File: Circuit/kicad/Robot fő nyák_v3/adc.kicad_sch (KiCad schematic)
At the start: 9 parts, among them U28 ADC1283, U29 ADC1283, U30 ADC1283, U31 ADS1115IDGS, U32 ADS1115IDGS, U33 ADS1115IDGS

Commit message: kicad i2c schematic updated: gyto i2c bugfixes, +add new datasheets
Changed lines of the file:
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@@
 (kicad_sch
-	(version 20231120)
+	(version 20250114)
 	(generator "eeschema")
-	(generator_version "8.0")
+	(generator_version "9.0")
 	(paper "A4")
 	(symbol

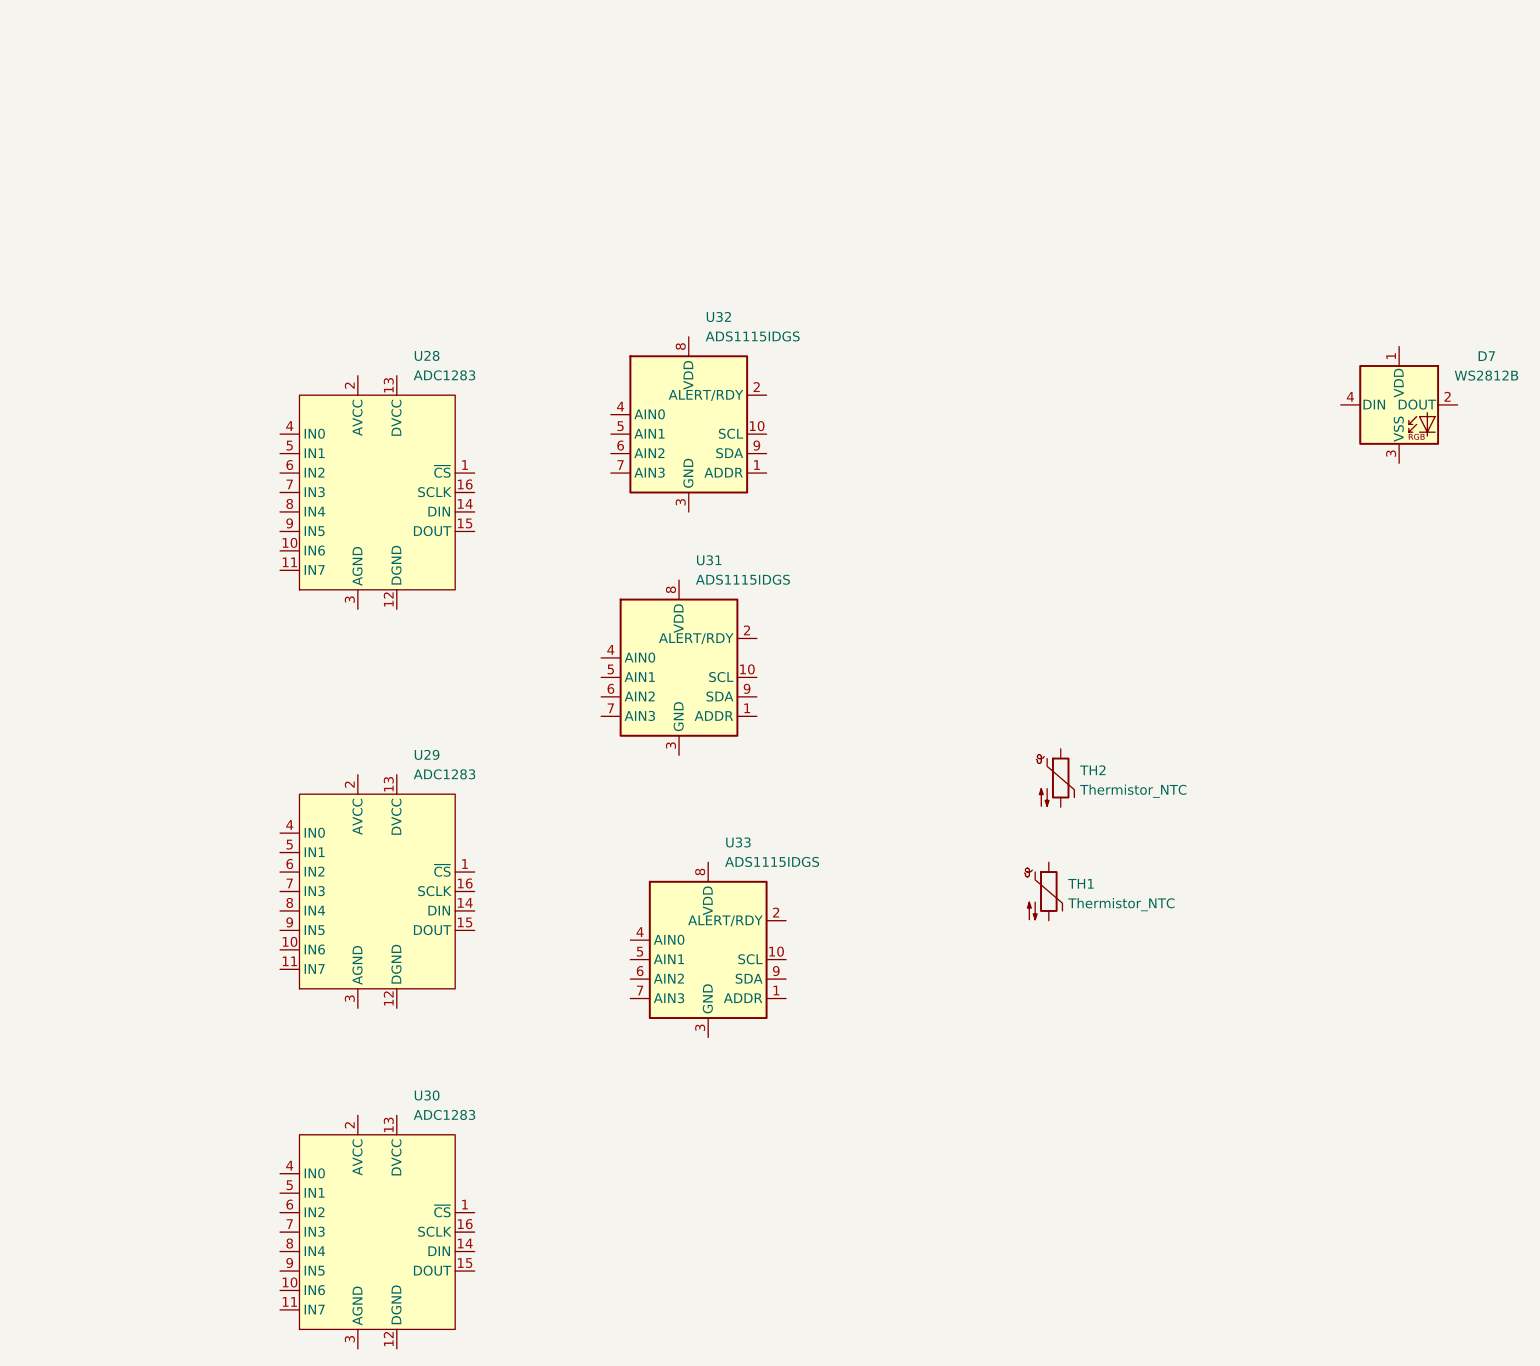
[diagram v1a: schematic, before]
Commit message: KICAD V3.01 Cleaned sheets + update + szekér modell add
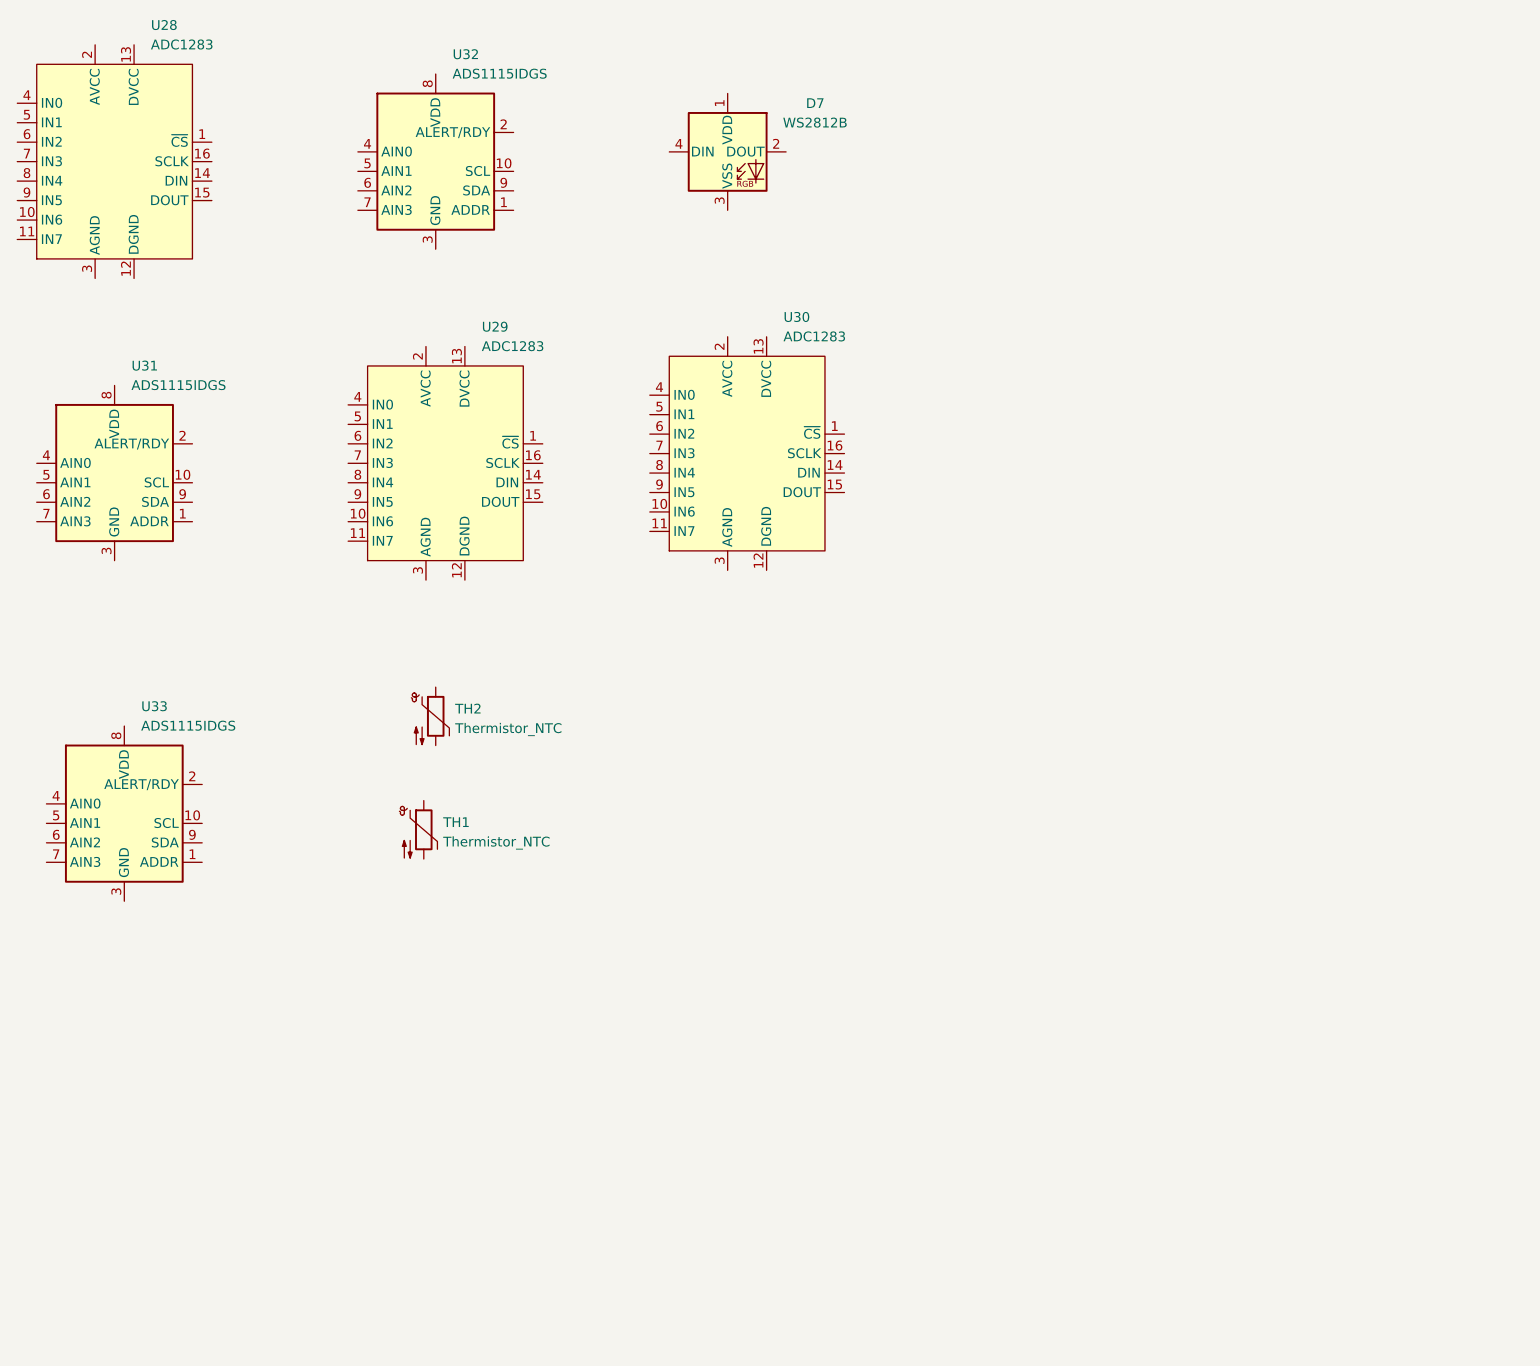
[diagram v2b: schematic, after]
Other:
- moved on the sheet: D7, TH1, TH2, U28, U29, U30, U31, U32, U33
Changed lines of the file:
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@@
 	(symbol
 		(lib_id "Analog_ADC:ADS1115IDGS")
-		(at 116.84 144.78 0)
+		(at 40.64 127 0)
 		(unit 1)
 		(exclude_from_sim no)
@@
 		(fields_autoplaced yes)
 		(property "Reference" "U33"
-			(at 119.0341 129.54 0)
+			(at 42.8341 111.76 0)
 			(effects
 				(font
@@
 		)
 		(property "Value" "ADS1115IDGS"
-			(at 119.0341 132.08 0)
+			(at 42.8341 114.3 0)
 			(effects
 				(font
@@
 		)
 		(property "Footprint" "Package_SO:TSSOP-10_3x3mm_P0.5mm"
-			(at 116.84 157.48 0)
+			(at 40.64 139.7 0)
 			(effects
 				(font
@@
 		)
 		(property "Datasheet" "http://www.ti.com/lit/ds/symlink/ads1113.pdf"
-			(at 115.57 167.64 0)
+			(at 39.37 149.86 0)
 			(effects
 				(font
@@
 		)
 		(property "Description" "Ultra-Small, Low-Power, I2C-Compatible, 860-SPS, 16-Bit ADCs With Internal Reference, Oscillator, and Programmable Comparator, VSSOP-10"
-			(at 116.84 144.78 0)
+			(at 40.64 127 0)
 			(effects
 				(font
@@
 	(symbol
 		(lib_id "Analog_ADC:ADC1283")
-		(at 73.66 83.82 0)
+		(at 39.37 40.64 0)
 		(unit 1)
 		(exclude_from_sim no)
@@
 		(fields_autoplaced yes)
 		(property "Reference" "U28"
-			(at 78.3941 66.04 0)
+			(at 44.1041 22.86 0)
 			(effects
 				(font
@@
 		)
 		(property "Value" "ADC1283"
-			(at 78.3941 68.58 0)
+			(at 44.1041 25.4 0)
 			(effects
 				(font
@@
 		)
 		(property "Footprint" "Package_SO:TSSOP-16_4.4x5mm_P0.65mm"
-			(at 73.66 104.14 0)
+			(at 39.37 60.96 0)
 			(effects
 				(font
@@
 		)
 		(property "Datasheet" "https://www.st.com/resource/en/datasheet/adc1283.pdf"
-			(at 73.66 83.82 0)
+			(at 39.37 40.64 0)
 			(effects
 				(font
@@
 		)
 		(property "Description" "Low power 8-channel single ended 12-bit SAR ADC, 50 ksps to 200 ksps, SPI, TSSOP-16"
-			(at 73.66 83.82 0)
+			(at 39.37 40.64 0)
 			(effects
 				(font
@@
 	(symbol
 		(lib_id "Analog_ADC:ADS1115IDGS")
-		(at 113.03 107.95 0)
+		(at 39.37 82.55 0)
 		(unit 1)
 		(exclude_from_sim no)
@@
 		(fields_autoplaced yes)
 		(property "Reference" "U31"
-			(at 115.2241 92.71 0)
+			(at 41.5641 67.31 0)
 			(effects
 				(font
@@
 		)
 		(property "Value" "ADS1115IDGS"
-			(at 115.2241 95.25 0)
+			(at 41.5641 69.85 0)
 			(effects
 				(font
@@
 		)
 		(property "Footprint" "Package_SO:TSSOP-10_3x3mm_P0.5mm"
-			(at 113.03 120.65 0)
+			(at 39.37 95.25 0)
 			(effects
 				(font
@@
 		)
 		(property "Datasheet" "http://www.ti.com/lit/ds/symlink/ads1113.pdf"
-			(at 111.76 130.81 0)
+			(at 38.1 105.41 0)
 			(effects
 				(font
@@
 		)
 		(property "Description" "Ultra-Small, Low-Power, I2C-Compatible, 860-SPS, 16-Bit ADCs With Internal Reference, Oscillator, and Programmable Comparator, VSSOP-10"
-			(at 113.03 107.95 0)
+			(at 39.37 82.55 0)
 			(effects
 				(font
@@
 	(symbol
 		(lib_id "Analog_ADC:ADC1283")
-		(at 73.66 135.89 0)
+		(at 82.55 80.01 0)
 		(unit 1)
 		(exclude_from_sim no)
@@
 		(fields_autoplaced yes)
 		(property "Reference" "U29"
-			(at 78.3941 118.11 0)
+			(at 87.2841 62.23 0)
 			(effects
 				(font
@@
 		)
 		(property "Value" "ADC1283"
-			(at 78.3941 120.65 0)
+			(at 87.2841 64.77 0)
 			(effects
 				(font
@@
 		)
 		(property "Footprint" "Package_SO:TSSOP-16_4.4x5mm_P0.65mm"
-			(at 73.66 156.21 0)
+			(at 82.55 100.33 0)
 			(effects
 				(font
@@
 		)
 		(property "Datasheet" "https://www.st.com/resource/en/datasheet/adc1283.pdf"
-			(at 73.66 135.89 0)
+			(at 82.55 80.01 0)
 			(effects
 				(font
@@
 		)
 		(property "Description" "Low power 8-channel single ended 12-bit SAR ADC, 50 ksps to 200 ksps, SPI, TSSOP-16"
-			(at 73.66 135.89 0)
+			(at 82.55 80.01 0)
 			(effects
 				(font
@@
 	(symbol
 		(lib_id "Analog_ADC:ADS1115IDGS")
-		(at 114.3 76.2 0)
+		(at 81.28 41.91 0)
 		(unit 1)
 		(exclude_from_sim no)
@@
 		(fields_autoplaced yes)
 		(property "Reference" "U32"
-			(at 116.4941 60.96 0)
+			(at 83.4741 26.67 0)
 			(effects
 				(font
@@
 		)
 		(property "Value" "ADS1115IDGS"
-			(at 116.4941 63.5 0)
+			(at 83.4741 29.21 0)
 			(effects
 				(font
@@
 		)
 		(property "Footprint" "Package_SO:TSSOP-10_3x3mm_P0.5mm"
-			(at 114.3 88.9 0)
+			(at 81.28 54.61 0)
 			(effects
 				(font
@@
 		)
 		(property "Datasheet" "http://www.ti.com/lit/ds/symlink/ads1113.pdf"
-			(at 113.03 99.06 0)
+			(at 80.01 64.77 0)
 			(effects
 				(font
@@
 		)
 		(property "Description" "Ultra-Small, Low-Power, I2C-Compatible, 860-SPS, 16-Bit ADCs With Internal Reference, Oscillator, and Programmable Comparator, VSSOP-10"
-			(at 114.3 76.2 0)
+			(at 81.28 41.91 0)
 			(effects
 				(font
@@
 	(symbol
 		(lib_id "LED:WS2812B")
-		(at 207.01 72.39 0)
+		(at 119.38 39.37 0)
 		(unit 1)
 		(exclude_from_sim no)
@@
 		(fields_autoplaced yes)
 		(property "Reference" "D7"
-			(at 218.44 66.0714 0)
+			(at 130.81 33.0514 0)
 			(effects
 				(font
@@
 		)
 		(property "Value" "WS2812B"
-			(at 218.44 68.6114 0)
+			(at 130.81 35.5914 0)
 			(effects
 				(font
@@
 		)
 		(property "Footprint" "LED_SMD:LED_WS2812B_PLCC4_5.0x5.0mm_P3.2mm"
-			(at 208.28 80.01 0)
+			(at 120.65 46.99 0)
 			(effects
 				(font
@@
 		)
 		(property "Datasheet" "https://cdn-shop.adafruit.com/datasheets/WS2812B.pdf"
-			(at 209.55 81.915 0)
+			(at 121.92 48.895 0)
 			(effects
 				(font
@@
 		)
 		(property "Description" "RGB LED with integrated controller"
-			(at 207.01 72.39 0)
+			(at 119.38 39.37 0)
 			(effects
 				(font
@@
 	(symbol
 		(lib_id "Device:Thermistor_NTC")
-		(at 162.8472 121.0811 0)
+		(at 81.28 113.03 0)
 		(unit 1)
 		(exclude_from_sim no)
@@
 		(fields_autoplaced yes)
 		(property "Reference" "TH2"
-			(at 165.3872 120.1285 0)
+			(at 83.82 112.0774 0)
 			(effects
 				(font
@@
 		)
 		(property "Value" "Thermistor_NTC"
-			(at 165.3872 122.6685 0)
+			(at 83.82 114.6174 0)
 			(effects
 				(font
@@
 		)
 		(property "Footprint" ""
-			(at 162.8472 119.8111 0)
+			(at 81.28 111.76 0)
 			(effects
 				(font
@@
 		)
 		(property "Datasheet" "~"
-			(at 162.8472 119.8111 0)
+			(at 81.28 111.76 0)
 			(effects
 				(font
@@
 		)
 		(property "Description" "Temperature dependent resistor, negative temperature coefficient"
-			(at 162.8472 121.0811 0)
+			(at 81.28 113.03 0)
 			(effects
 				(font
@@
 	(symbol
 		(lib_id "Device:Thermistor_NTC")
-		(at 161.29 135.89 0)
+		(at 79.7228 127.8389 0)
 		(unit 1)
 		(exclude_from_sim no)
@@
 		(fields_autoplaced yes)
 		(property "Reference" "TH1"
-			(at 163.83 134.9374 0)
+			(at 82.2628 126.8863 0)
 			(effects
 				(font
@@
 		)
 		(property "Value" "Thermistor_NTC"
-			(at 163.83 137.4774 0)
+			(at 82.2628 129.4263 0)
 			(effects
 				(font
@@
 		)
 		(property "Footprint" ""
-			(at 161.29 134.62 0)
+			(at 79.7228 126.5689 0)
 			(effects
 				(font
@@
 		)
 		(property "Datasheet" "~"
-			(at 161.29 134.62 0)
+			(at 79.7228 126.5689 0)
 			(effects
 				(font
@@
 		)
 		(property "Description" "Temperature dependent resistor, negative temperature coefficient"
-			(at 161.29 135.89 0)
+			(at 79.7228 127.8389 0)
 			(effects
 				(font
@@
 	(symbol
 		(lib_id "Analog_ADC:ADC1283")
-		(at 73.66 180.34 0)
+		(at 121.92 78.74 0)
 		(unit 1)
 		(exclude_from_sim no)
@@
 		(fields_autoplaced yes)
 		(property "Reference" "U30"
-			(at 78.3941 162.56 0)
+			(at 126.6541 60.96 0)
 			(effects
 				(font
@@
 		)
 		(property "Value" "ADC1283"
-			(at 78.3941 165.1 0)
+			(at 126.6541 63.5 0)
 			(effects
 				(font
@@
 		)
 		(property "Footprint" "Package_SO:TSSOP-16_4.4x5mm_P0.65mm"
-			(at 73.66 200.66 0)
+			(at 121.92 99.06 0)
 			(effects
 				(font
@@
 		)
 		(property "Datasheet" "https://www.st.com/resource/en/datasheet/adc1283.pdf"
-			(at 73.66 180.34 0)
+			(at 121.92 78.74 0)
 			(effects
 				(font
@@
 		)
 		(property "Description" "Low power 8-channel single ended 12-bit SAR ADC, 50 ksps to 200 ksps, SPI, TSSOP-16"
-			(at 73.66 180.34 0)
-			(effects
-				(font
+			(at 121.92 78.74 0)
+			(effects
+				(font
